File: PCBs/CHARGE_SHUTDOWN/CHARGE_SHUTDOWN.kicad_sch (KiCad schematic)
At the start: 29 parts, among them J1 PUSH_ROTATE, J2 PACK, J3 SMPS, J4 RESET, J5 HV, J6 AC_RELAY, J7 Conn_01x01_Female, Q1 IRF9540N, Q2 IRF740, U1 ADJ14012, U2 ADJ14012

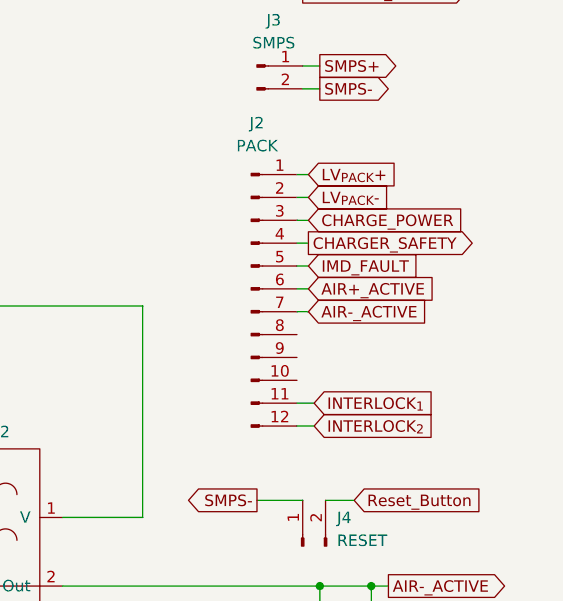
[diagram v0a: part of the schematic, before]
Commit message: update: schematics and wirings to current state
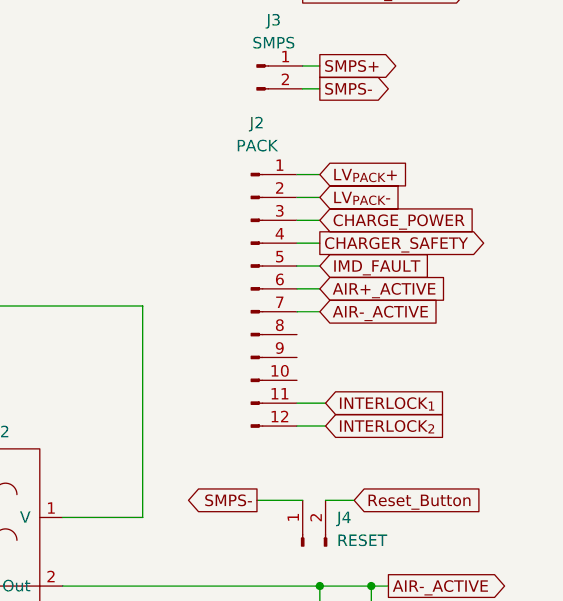
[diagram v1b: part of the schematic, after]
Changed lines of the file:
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@@
     (stroke (width 0) (type default) (color 0 0 0 0))
+  )
+  (wire (pts (xy 238.125 55.88) (xy 235.585 55.88))
+    (stroke (width 0.5) (type default) (color 132 132 132 1))
   )
   (wire (pts (xy 101.6 78.74) (xy 98.425 78.74))
@@
     (stroke (width 0) (type default) (color 0 0 0 0))
   )
-  (wire (pts (xy 236.855 40.64) (xy 235.585 40.64))
-    (stroke (width 0) (type default) (color 0 0 0 0))
+  (wire (pts (xy 238.125 40.64) (xy 235.585 40.64))
+    (stroke (width 0.5) (type default) (color 194 0 0 1))
   )
   (wire (pts (xy 161.925 36.83) (xy 159.385 36.83))
@@
     (stroke (width 0) (type default) (color 0 0 0 0))
   )
-  (wire (pts (xy 236.855 43.18) (xy 235.585 43.18))
-    (stroke (width 0) (type default) (color 0 0 0 0))
+  (wire (pts (xy 238.125 43.18) (xy 235.585 43.18))
+    (stroke (width 0.5) (type default) (color 0 0 0 1))
   )
   (wire (pts (xy 159.385 41.91) (xy 159.385 44.45))
@@
     (stroke (width 0) (type default) (color 0 0 0 0))
   )
-  (wire (pts (xy 236.855 48.26) (xy 235.585 48.26))
-    (stroke (width 0) (type default) (color 0 0 0 0))
-  )
-  (wire (pts (xy 236.855 45.72) (xy 235.585 45.72))
-    (stroke (width 0) (type default) (color 0 0 0 0))
+  (wire (pts (xy 238.125 45.72) (xy 235.585 45.72))
+    (stroke (width 0.5) (type default) (color 194 0 0 1))
+  )
+  (wire (pts (xy 238.125 48.26) (xy 235.585 48.26))
+    (stroke (width 0.5) (type default) (color 0 0 255 1))
   )
   (wire (pts (xy 220.345 91.44) (xy 219.075 91.44))
@@
     (stroke (width 0) (type default) (color 0 0 0 0))
   )
-  (wire (pts (xy 237.49 68.58) (xy 235.585 68.58))
-    (stroke (width 0) (type default) (color 0 0 0 0))
-  )
-  (wire (pts (xy 237.49 66.04) (xy 235.585 66.04))
-    (stroke (width 0) (type default) (color 0 0 0 0))
+  (wire (pts (xy 238.76 66.04) (xy 235.585 66.04))
+    (stroke (width 0.5) (type default) (color 194 194 194 0.45))
   )
   (wire (pts (xy 133.35 93.98) (xy 131.445 93.98))
     (stroke (width 0) (type default) (color 0 0 0 0))
   )
-  (wire (pts (xy 236.855 50.8) (xy 235.585 50.8))
-    (stroke (width 0) (type default) (color 0 0 0 0))
+  (wire (pts (xy 238.125 50.8) (xy 235.585 50.8))
+    (stroke (width 0.5) (type default) (color 72 72 0 1))
   )
   (wire (pts (xy 78.74 101.6) (xy 76.2 101.6))
@@
     (stroke (width 0) (type default) (color 0 0 0 0))
   )
-  (wire (pts (xy 236.855 53.34) (xy 235.585 53.34))
-    (stroke (width 0) (type default) (color 0 0 0 0))
+  (wire (pts (xy 238.125 53.34) (xy 235.585 53.34))
+    (stroke (width 0.5) (type default) (color 132 132 132 1))
   )
   (wire (pts (xy 163.83 68.58) (xy 167.005 68.58))
@@
     (stroke (width 0) (type default) (color 0 0 0 0))
   )
-  (wire (pts (xy 236.855 55.88) (xy 235.585 55.88))
-    (stroke (width 0) (type default) (color 0 0 0 0))
-  )
   (wire (pts (xy 142.24 93.98) (xy 140.97 93.98))
     (stroke (width 0) (type default) (color 0 0 0 0))
@@
   (wire (pts (xy 133.35 55.245) (xy 218.44 55.245))
     (stroke (width 0) (type default) (color 0 0 0 0))
+  )
+  (wire (pts (xy 238.76 68.58) (xy 235.585 68.58))
+    (stroke (width 0.5) (type default) (color 194 194 194 0.45))
   )
   (wire (pts (xy 125.7808 141.9352) (xy 201.9808 141.9352))
@@
     )
   )
-  (global_label "LV_{PACK}+" (shape input) (at 236.855 40.64 0) (fields_autoplaced)
-    (effects (font (size 1.27 1.27)) (justify left))
-    (property "Intersheet References" "${INTERSHEET_REFS}" (id 0) (at 246.876 40.5606 0)
+  (global_label "LV_{PACK}+" (shape input) (at 238.125 40.64 0) (fields_autoplaced)
+    (effects (font (size 1.27 1.27)) (justify left))
+    (property "Intersheet References" "${INTERSHEET_REFS}" (id 0) (at 248.146 40.5606 0)
       (effects (font (size 1.27 1.27)) (justify left) hide)
     )
@@
     )
   )
-  (global_label "LV_{PACK}-" (shape input) (at 236.855 43.18 0) (fields_autoplaced)
-    (effects (font (size 1.27 1.27)) (justify left))
-    (property "Intersheet References" "${INTERSHEET_REFS}" (id 0) (at 246.876 43.1006 0)
+  (global_label "LV_{PACK}-" (shape input) (at 238.125 43.18 0) (fields_autoplaced)
+    (effects (font (size 1.27 1.27)) (justify left))
+    (property "Intersheet References" "${INTERSHEET_REFS}" (id 0) (at 248.146 43.1006 0)
       (effects (font (size 1.27 1.27)) (justify left) hide)
     )
@@
     )
   )
-  (global_label "AIR+_ACTIVE" (shape input) (at 236.855 53.34 0) (fields_autoplaced)
-    (effects (font (size 1.27 1.27)) (justify left))
-    (property "Intersheet References" "${INTERSHEET_REFS}" (id 0) (at 250.94 53.2606 0)
+  (global_label "AIR+_ACTIVE" (shape input) (at 238.125 53.34 0) (fields_autoplaced)
+    (effects (font (size 1.27 1.27)) (justify left))
+    (property "Intersheet References" "${INTERSHEET_REFS}" (id 0) (at 252.21 53.2606 0)
       (effects (font (size 1.27 1.27)) (justify left) hide)
     )
@@
     )
   )
-  (global_label "CHARGE_POWER" (shape input) (at 236.855 45.72 0) (fields_autoplaced)
-    (effects (font (size 1.27 1.27)) (justify left))
-    (property "Intersheet References" "${INTERSHEET_REFS}" (id 0) (at 254.0848 45.6406 0)
+  (global_label "CHARGE_POWER" (shape input) (at 238.125 45.72 0) (fields_autoplaced)
+    (effects (font (size 1.27 1.27)) (justify left))
+    (property "Intersheet References" "${INTERSHEET_REFS}" (id 0) (at 255.3548 45.6406 0)
       (effects (font (size 1.27 1.27)) (justify left) hide)
     )
@@
     )
   )
-  (global_label "CHARGER_SAFETY" (shape output) (at 236.855 48.26 0) (fields_autoplaced)
-    (effects (font (size 1.27 1.27)) (justify left))
-    (property "Intersheet References" "${INTERSHEET_REFS}" (id 0) (at 255.4757 48.1806 0)
+  (global_label "CHARGER_SAFETY" (shape output) (at 238.125 48.26 0) (fields_autoplaced)
+    (effects (font (size 1.27 1.27)) (justify left))
+    (property "Intersheet References" "${INTERSHEET_REFS}" (id 0) (at 256.7457 48.1806 0)
       (effects (font (size 1.27 1.27)) (justify left) hide)
     )
@@
     )
   )
-  (global_label "INTERLOCK_{2}" (shape input) (at 237.49 68.58 0) (fields_autoplaced)
-    (effects (font (size 1.27 1.27)) (justify left))
-    (property "Intersheet References" "${INTERSHEET_REFS}" (id 0) (at 251.0912 68.5006 0)
+  (global_label "INTERLOCK_{2}" (shape input) (at 238.76 68.58 0) (fields_autoplaced)
+    (effects (font (size 1.27 1.27)) (justify left))
+    (property "Intersheet References" "${INTERSHEET_REFS}" (id 0) (at 252.3612 68.5006 0)
       (effects (font (size 1.27 1.27)) (justify left) hide)
     )
@@
     )
   )
-  (global_label "AIR-_ACTIVE" (shape input) (at 236.855 55.88 0) (fields_autoplaced)
-    (effects (font (size 1.27 1.27)) (justify left))
-    (property "Intersheet References" "${INTERSHEET_REFS}" (id 0) (at 250.94 55.8006 0)
+  (global_label "AIR-_ACTIVE" (shape input) (at 238.125 55.88 0) (fields_autoplaced)
+    (effects (font (size 1.27 1.27)) (justify left))
+    (property "Intersheet References" "${INTERSHEET_REFS}" (id 0) (at 252.21 55.8006 0)
       (effects (font (size 1.27 1.27)) (justify left) hide)
     )
@@
     )
   )
-  (global_label "INTERLOCK_{1}" (shape input) (at 237.49 66.04 0) (fields_autoplaced)
-    (effects (font (size 1.27 1.27)) (justify left))
-    (property "Intersheet References" "${INTERSHEET_REFS}" (id 0) (at 251.0912 65.9606 0)
-      (effects (font (size 1.27 1.27)) (justify left) hide)
-    )
-  )
-  (global_label "IMD_FAULT" (shape input) (at 236.855 50.8 0) (fields_autoplaced)
-    (effects (font (size 1.27 1.27)) (justify left))
-    (property "Intersheet References" "${INTERSHEET_REFS}" (id 0) (at 249.0652 50.7206 0)
-      (effects (font (size 1.27 1.27)) (justify left) hide)
-    )
+  (global_label "INTERLOCK_{1}" (shape input) (at 238.76 66.04 0) (fields_autoplaced)
+    (effects (font (size 1.27 1.27)) (justify left))
+    (property "Intersheet References" "${INTERSHEET_REFS}" (id 0) (at 252.3612 65.9606 0)
+      (effects (font (size 1.27 1.27)) (justify left) hide)
+    )
+  )
+  (global_label "IMD_FAULT" (shape input) (at 238.125 50.8 0) (fields_autoplaced)
+    (effects (font (size 1.27 1.27)) (justify left))
+    (property "Intersheet References" "${INTERSHEET_REFS}" (id 0) (at 250.3352 50.7206 0)
+      (effects (font (size 1.27 1.27)) (justify left) hide)
+    )
